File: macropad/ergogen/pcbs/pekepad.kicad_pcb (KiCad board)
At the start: 2 copper layers, 188.3 x 42 mm, 37 parts

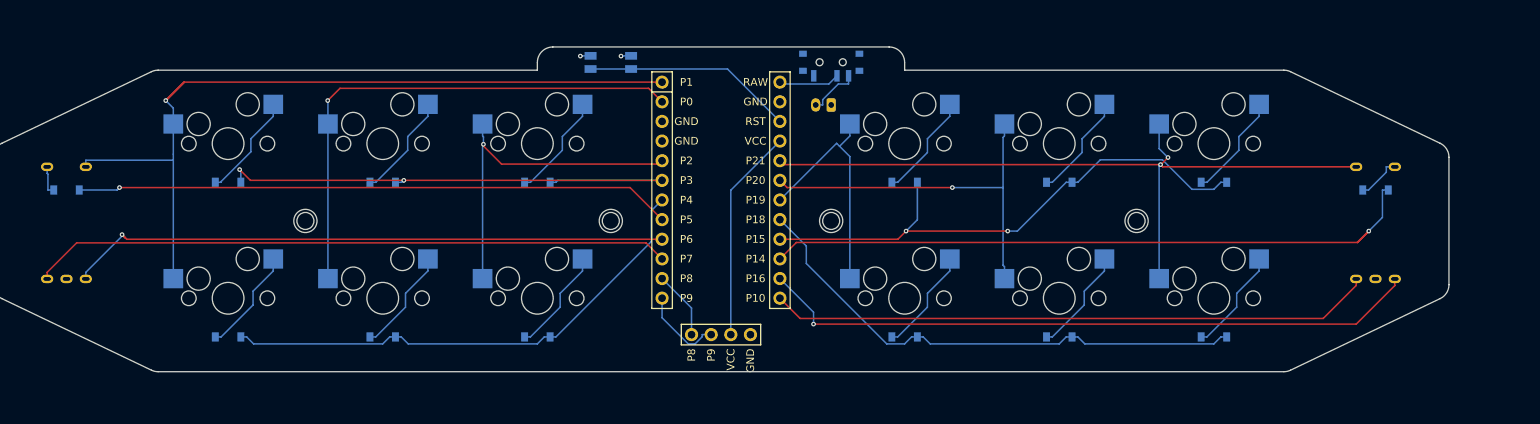
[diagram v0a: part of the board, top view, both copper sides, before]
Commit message: batt connector space fix
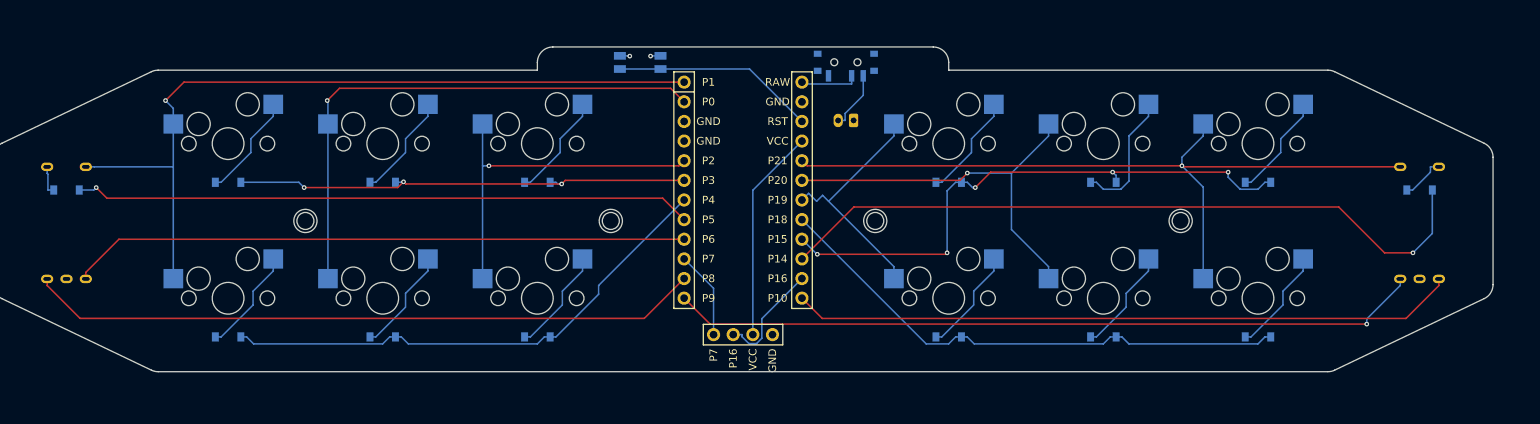
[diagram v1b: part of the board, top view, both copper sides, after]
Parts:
- moved D10 5.70 mm to (213.2, 105.0)
- moved D11 5.70 mm to (193.2, 125.0)
- moved D12 5.70 mm to (193.2, 105.0)
- moved D14 5.70 mm to (254.1, 106.0)
- moved D7 5.70 mm to (233.2, 125.0)
- moved D8 5.70 mm to (233.2, 105.0)
- moved D9 5.70 mm to (213.2, 125.0)
- moved MH3 5.70 mm to (223.2, 110.0)
- moved MH4 5.70 mm to (183.7, 110.0)
- moved RE2 5.70 mm to (254.1, 110.0)
- moved S10 5.70 mm to (213.2, 100.0)
- moved S11 5.70 mm to (193.2, 120.0)
- moved S12 5.70 mm to (193.2, 100.0)
- moved S7 5.70 mm to (233.2, 120.0)
- moved S8 5.70 mm to (233.2, 100.0)
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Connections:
- DISP1 pad 1: P8 -> P7
- DISP1 pad 2: P9 -> P16
- RE1 pad C: P7 -> P8
- RE2 pad A: P16 -> P10
- RE2 pad C: P10 -> P9
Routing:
- net P9: track 10.9 -> 97.3 mm, vias 0 -> 1
- net P8: track 8.83 -> 87.1 mm
- net P7: track 82.8 -> 11.4 mm
- net P16: track 85.8 -> 14.5 mm, vias 1 -> 0
- net P3: track 73.2 -> 60.9 mm, vias 2 -> 3
- net P1: track 114.3 -> 102.8 mm
- net P10: track 78.2 -> 86.1 mm
- net P21: track 96.1 -> 100.0 mm, vias 2 -> 1
- net P15: track 70.9 -> 74.3 mm, vias 2 -> 5
- net mirror_middle_top: track 13.6 -> 16.7 mm
- net P0: track 67.7 -> 70.6 mm
- net P5: track 77.2 -> 80.1 mm
- net P20: track 49.4 -> 51.5 mm
- net P2: track 44.6 -> 46.3 mm
- net P18: track 67.6 -> 69.2 mm
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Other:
- board size 188.3 x 42 mm -> 194 x 42 mm

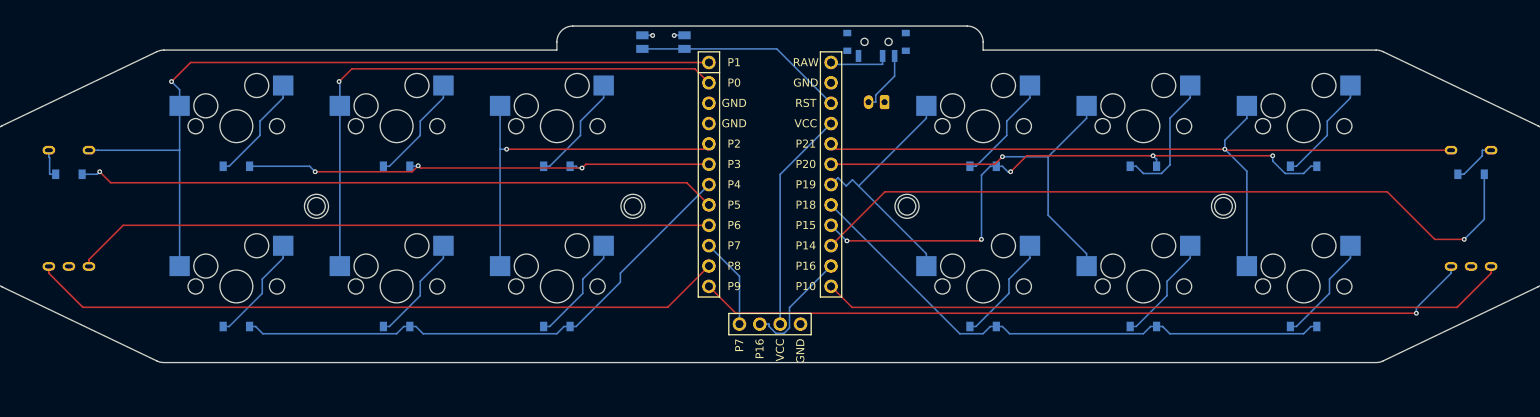
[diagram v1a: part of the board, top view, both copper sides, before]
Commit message: Freeing up Pin P1 (SC) for Nice View Adding some 3D models for kicad
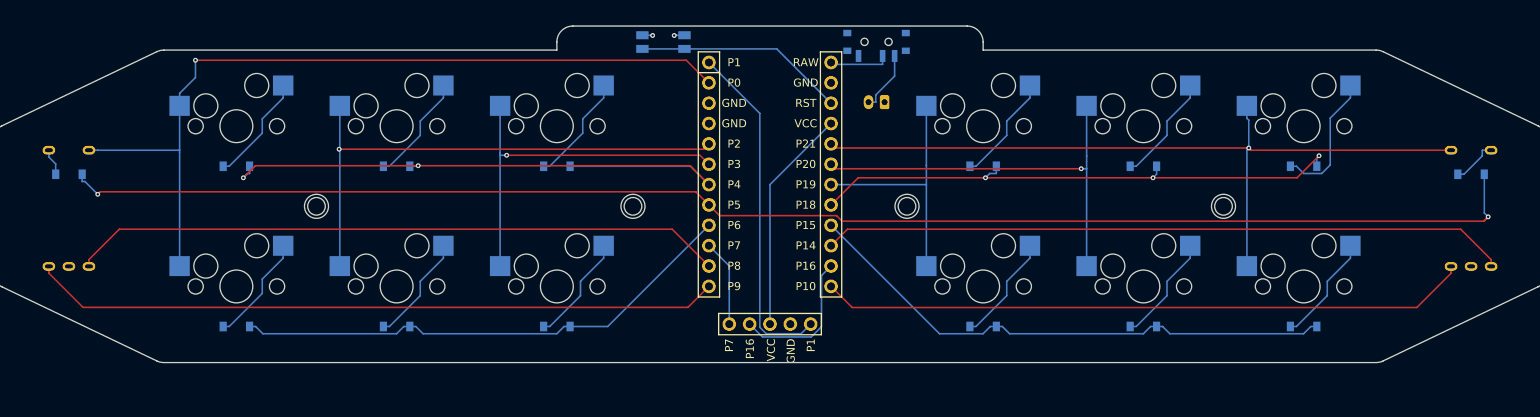
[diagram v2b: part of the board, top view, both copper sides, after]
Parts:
- DISP1: footprint ceoloide:display_ssd1306 -> ceoloide:display_nice_view
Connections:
- D1 pad 1: P4 -> P6
- D10 pad 1: P15 -> P18
- D11 pad 1: P18 -> P15
- D12 pad 1: P15 -> P18
- D14 pad 1: P14 -> P5
- D2 pad 1: P3 -> P4
- D3 pad 1: P4 -> P6
- D4 pad 1: P3 -> P4
- D5 pad 1: P4 -> P6
- D6 pad 1: P3 -> P4
- D7 pad 1: P18 -> P15
- D8 pad 1: P15 -> P18
- D9 pad 1: P18 -> P15
- RE1 pad A: P6 -> P8
- RE1 pad C: P8 -> P9
- RE1 pad S2: P1 -> P0
- RE2 pad A: P10 -> P14
- RE2 pad C: P9 -> P10
- S1 pad 1: P1 -> P0
- S2 pad 1: P1 -> P0
- S3 pad 1: P0 -> P2
- S4 pad 1: P0 -> P2
- S5 pad 1: P2 -> P3
- S6 pad 1: P2 -> P3
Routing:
- net P5: track 80.1 -> 187.5 mm, vias 1 -> 2
- net P1: track 102.8 -> 42.9 mm, vias 1 -> 0
- net P0: track 70.6 -> 103.1 mm
- net P2: track 46.3 -> 66.5 mm
- net P6: track 80.0 -> 64.1 mm
- net P3: track 60.9 -> 46.5 mm, vias 3 -> 1
- net P4: track 66.8 -> 81.0 mm, vias 0 -> 2
- net P9: track 97.3 -> 86.1 mm, vias 1 -> 0
- net P14: track 93.4 -> 85.7 mm, vias 1 -> 0
- net P15: track 74.3 -> 68.1 mm, vias 5 -> 0
- net P8: track 87.1 -> 81.7 mm
- net P10: track 86.1 -> 81.1 mm
- net P16: track 14.5 -> 18.2 mm
- net mirror_outer_top: track 13.6 -> 16.7 mm
- net mirror_middle_top: track 16.7 -> 13.6 mm
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
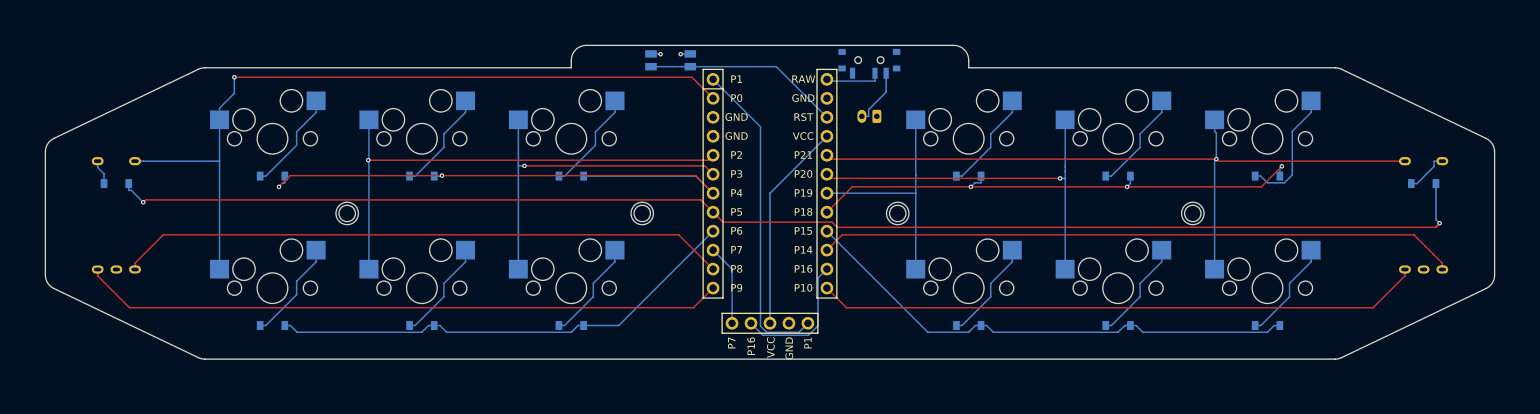
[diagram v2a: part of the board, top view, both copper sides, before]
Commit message: Ergogen: Updating assigned pins Ergogen: Renaming pins names to NiceNano Pings RMK: Updating assigned pins RMK: Always clear storage, temporary RMK: Trying to fix vial layout
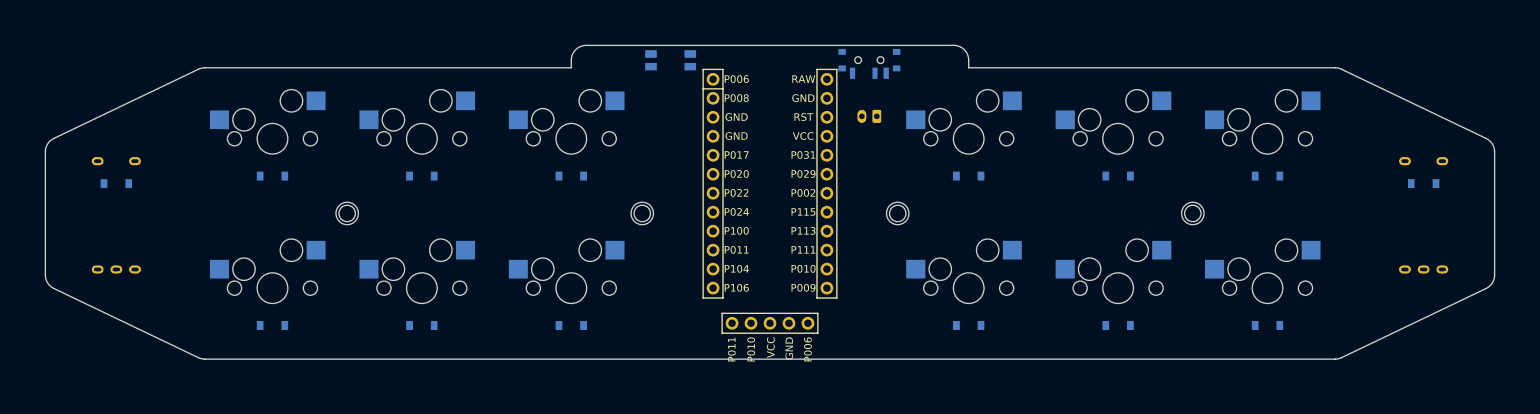
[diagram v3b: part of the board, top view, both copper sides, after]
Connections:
- net P0 renamed P008
- net P1 renamed P006
- net P10 renamed P009
- net P14 renamed P111
- net P15 renamed P113
- net P16 renamed P010
- net P18 renamed P115
- net P19 renamed P002
- net P2 renamed P017
- net P20 renamed P029
- net P21 renamed P031
- net P3 renamed P020
- net P4 renamed P022
- net P5 renamed P024
- net P6 renamed P100
- net P7 renamed P011
- net P8 renamed P104
- net P9 renamed P106
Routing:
- net P024: track 187.5 -> 0.00 mm, vias 2 -> 0
- net P008: track 103.1 -> 0.00 mm, vias 1 -> 0
- net P031: track 97.9 -> 0.00 mm, vias 1 -> 0
- net P106: track 86.1 -> 0.00 mm
- net P111: track 85.7 -> 0.00 mm
- net P104: track 81.7 -> 0.00 mm
- net P009: track 81.1 -> 0.00 mm
- net P022: track 81.0 -> 0.00 mm, vias 2 -> 0
- net P115: track 69.0 -> 0.00 mm, vias 3 -> 0
- net P113: track 68.1 -> 0.00 mm
- net P017: track 66.5 -> 0.00 mm, vias 1 -> 0
- net P100: track 64.1 -> 0.00 mm
- net P029: track 52.1 -> 0.00 mm, vias 1 -> 0
- net P020: track 46.5 -> 0.00 mm, vias 1 -> 0
- net P006: track 42.9 -> 0.00 mm
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
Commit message: Ergogen: increasing encoder hole
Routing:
- net P024: track 0.00 -> 183.9 mm, vias 0 -> 2
- net P008: track 0.00 -> 103.2 mm, vias 0 -> 1
- net P031: track 0.00 -> 97.9 mm, vias 0 -> 1
- net P106: track 0.00 -> 86.1 mm
- net P111: track 0.00 -> 85.7 mm
- net P104: track 0.00 -> 81.7 mm
- net P009: track 0.00 -> 81.1 mm
- net P115: track 0.00 -> 69.3 mm, vias 0 -> 3
- net P113: track 0.00 -> 68.1 mm
- net P017: track 0.00 -> 66.8 mm, vias 0 -> 1
- net P100: track 0.00 -> 64.1 mm
- net P022: track 0.00 -> 61.9 mm, vias 0 -> 3
- net P029: track 0.00 -> 52.3 mm, vias 0 -> 1
- net P020: track 0.00 -> 46.8 mm, vias 0 -> 1
- net P006: track 0.00 -> 42.9 mm
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
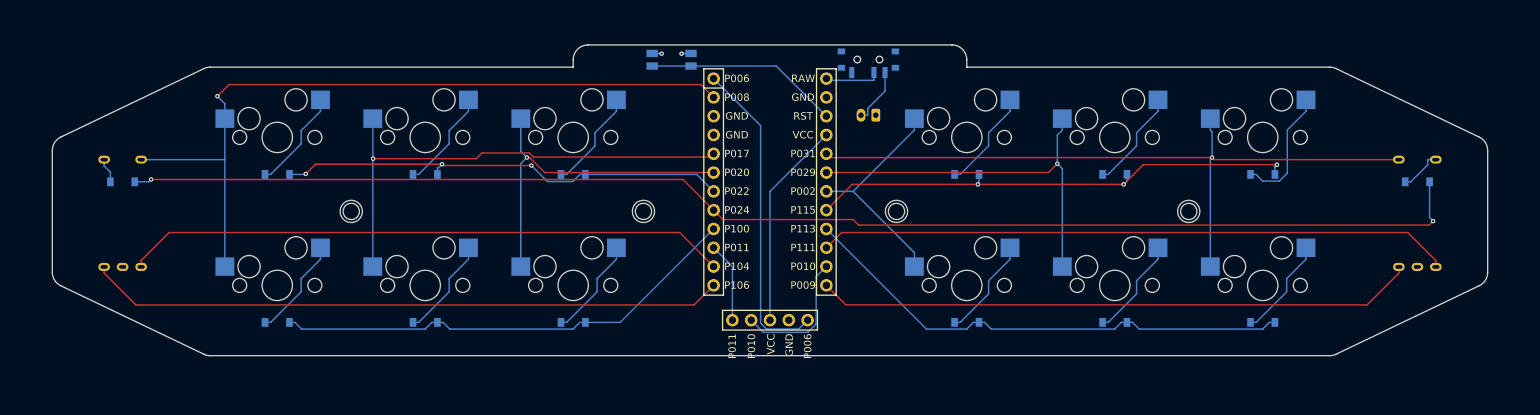
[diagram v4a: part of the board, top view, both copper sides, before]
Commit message: Inner case verical spacing Cutout for USB, reset and power Switchplate sides support
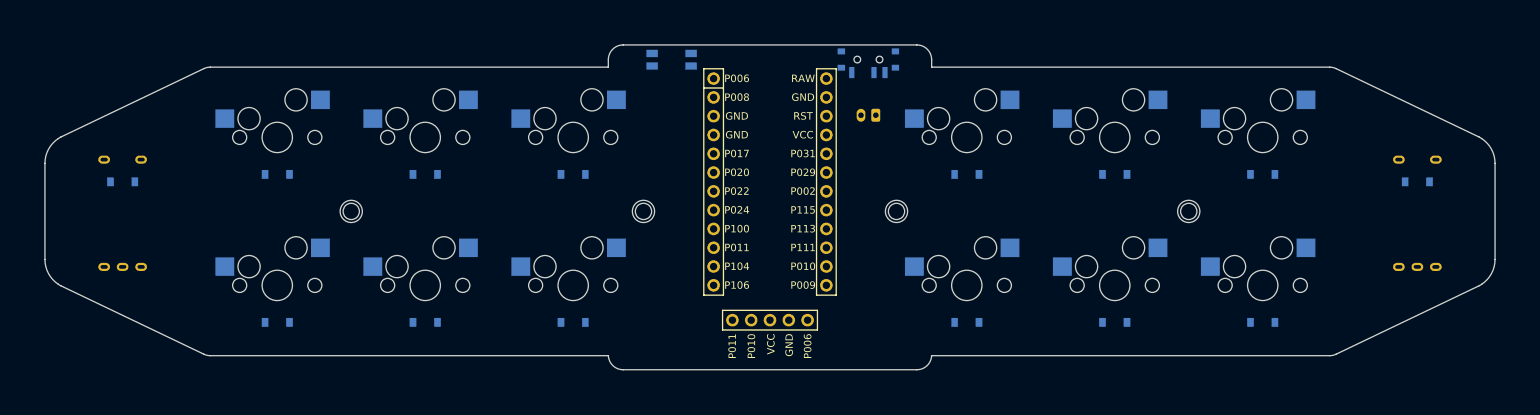
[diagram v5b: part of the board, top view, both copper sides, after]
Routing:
- net P024: track 183.9 -> 0.00 mm, vias 2 -> 0
- net P008: track 103.2 -> 0.00 mm, vias 1 -> 0
- net P031: track 97.9 -> 0.00 mm, vias 1 -> 0
- net P106: track 86.1 -> 0.00 mm
- net P111: track 85.7 -> 0.00 mm
- net P104: track 81.7 -> 0.00 mm
- net P009: track 81.1 -> 0.00 mm
- net P115: track 69.3 -> 0.00 mm, vias 3 -> 0
- net P113: track 68.1 -> 0.00 mm
- net P017: track 66.8 -> 0.00 mm, vias 1 -> 0
- net P100: track 64.1 -> 0.00 mm
- net P022: track 61.9 -> 0.00 mm, vias 3 -> 0
- net P029: track 52.3 -> 0.00 mm, vias 1 -> 0
- net P020: track 46.8 -> 0.00 mm, vias 1 -> 0
- net P006: track 42.9 -> 0.00 mm
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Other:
- board size 194 x 42 mm -> 196 x 43.9 mm
